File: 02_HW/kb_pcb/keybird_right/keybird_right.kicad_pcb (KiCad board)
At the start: 2 copper layers, 152.4 x 148.3 mm, 79 parts, among them J1 Adafruit_Feather_16_pin, J2 Adafruit_feather_12_pin, J4 FTDI UART, SW1 SW_Push, SW10 SW_Push, SW11 SW_Push, SW12 SW_Push, SW13 SW_Push, SW14 SW_Push, SW15 SW_Push, SW16 SW_Push, SW17 SW_Push, SW18 SW_Push, SW19 SW_Push, SW2 SW_Push, SW20 SW_Push, SW21 SW_Push, SW22 SW_Push, SW23 SW_Push, SW24 SW_Push, SW25 SW_Push, SW26 SW_Push, SW27 SW_Push, SW28 SW_Push, SW29 SW_Push, SW3 SW_Push, SW30 SW_Push, SW4 SW_Push, SW5 Power enable, SW6 SW_Push, SW7 SW_Push, SW8 SW_Push, SW9 SW_Push

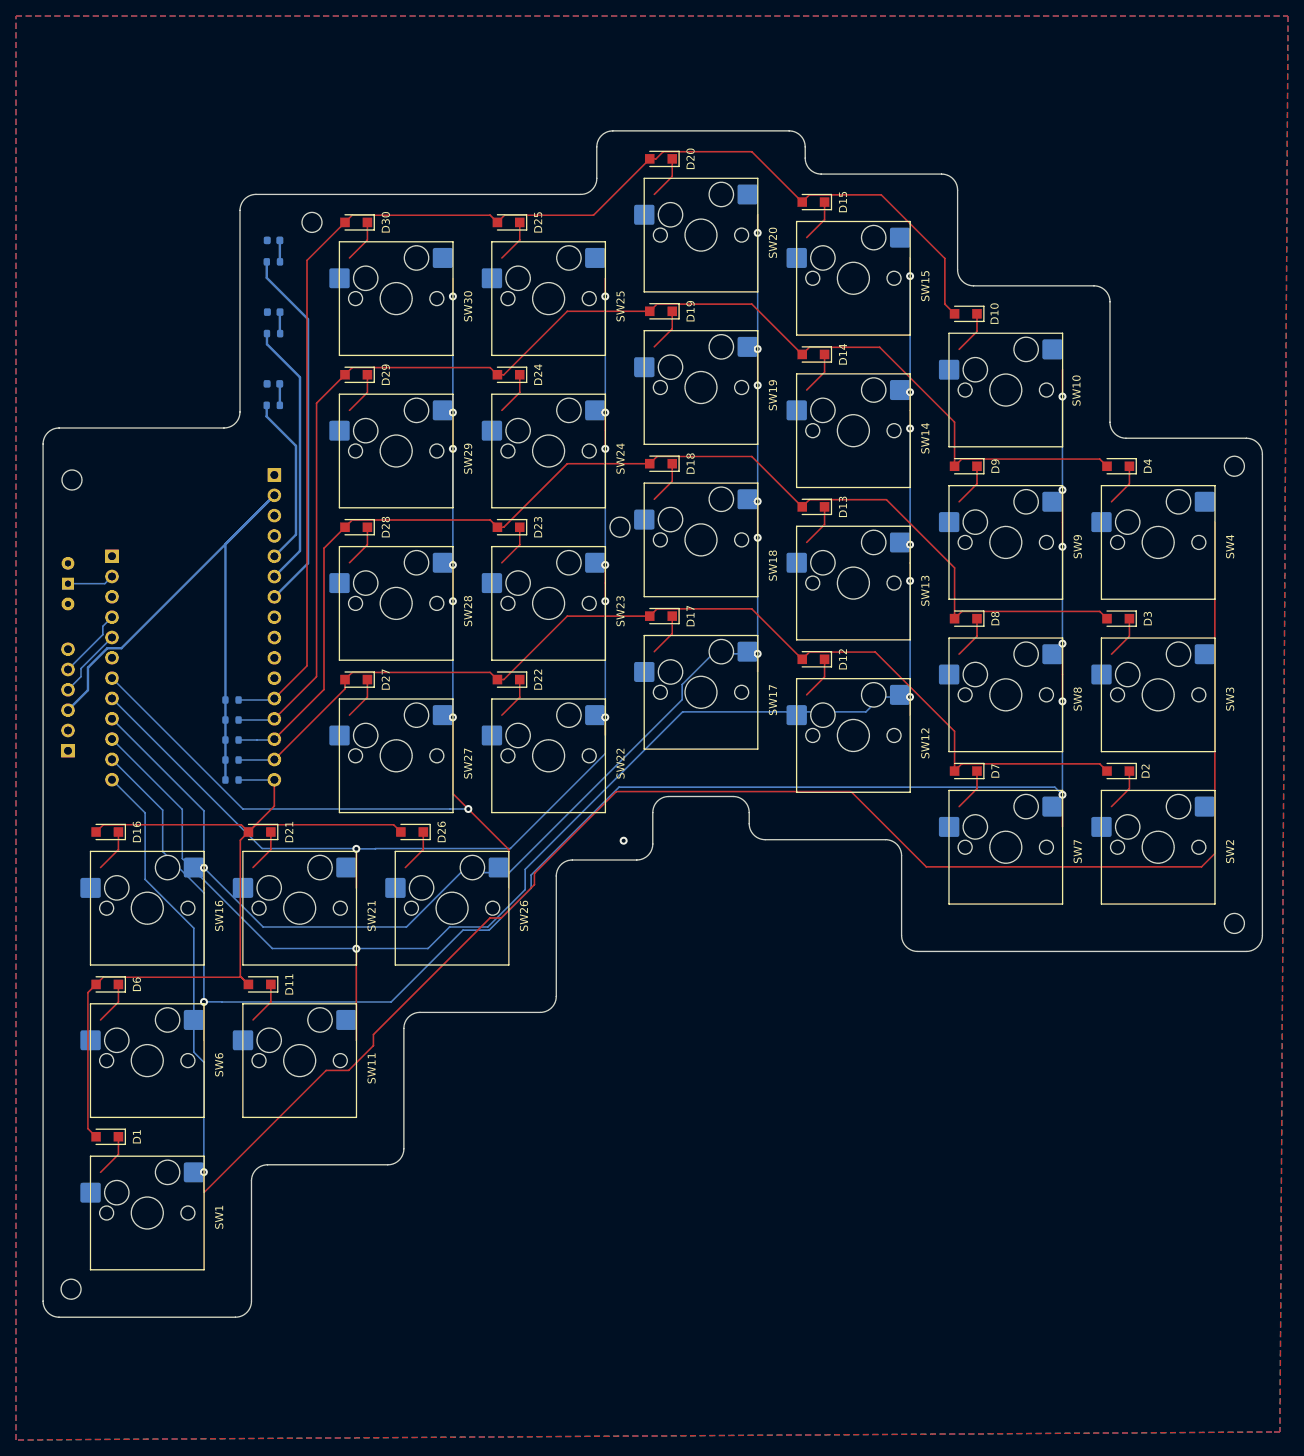
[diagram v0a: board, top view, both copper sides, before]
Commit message: left and right board pass design rule checks
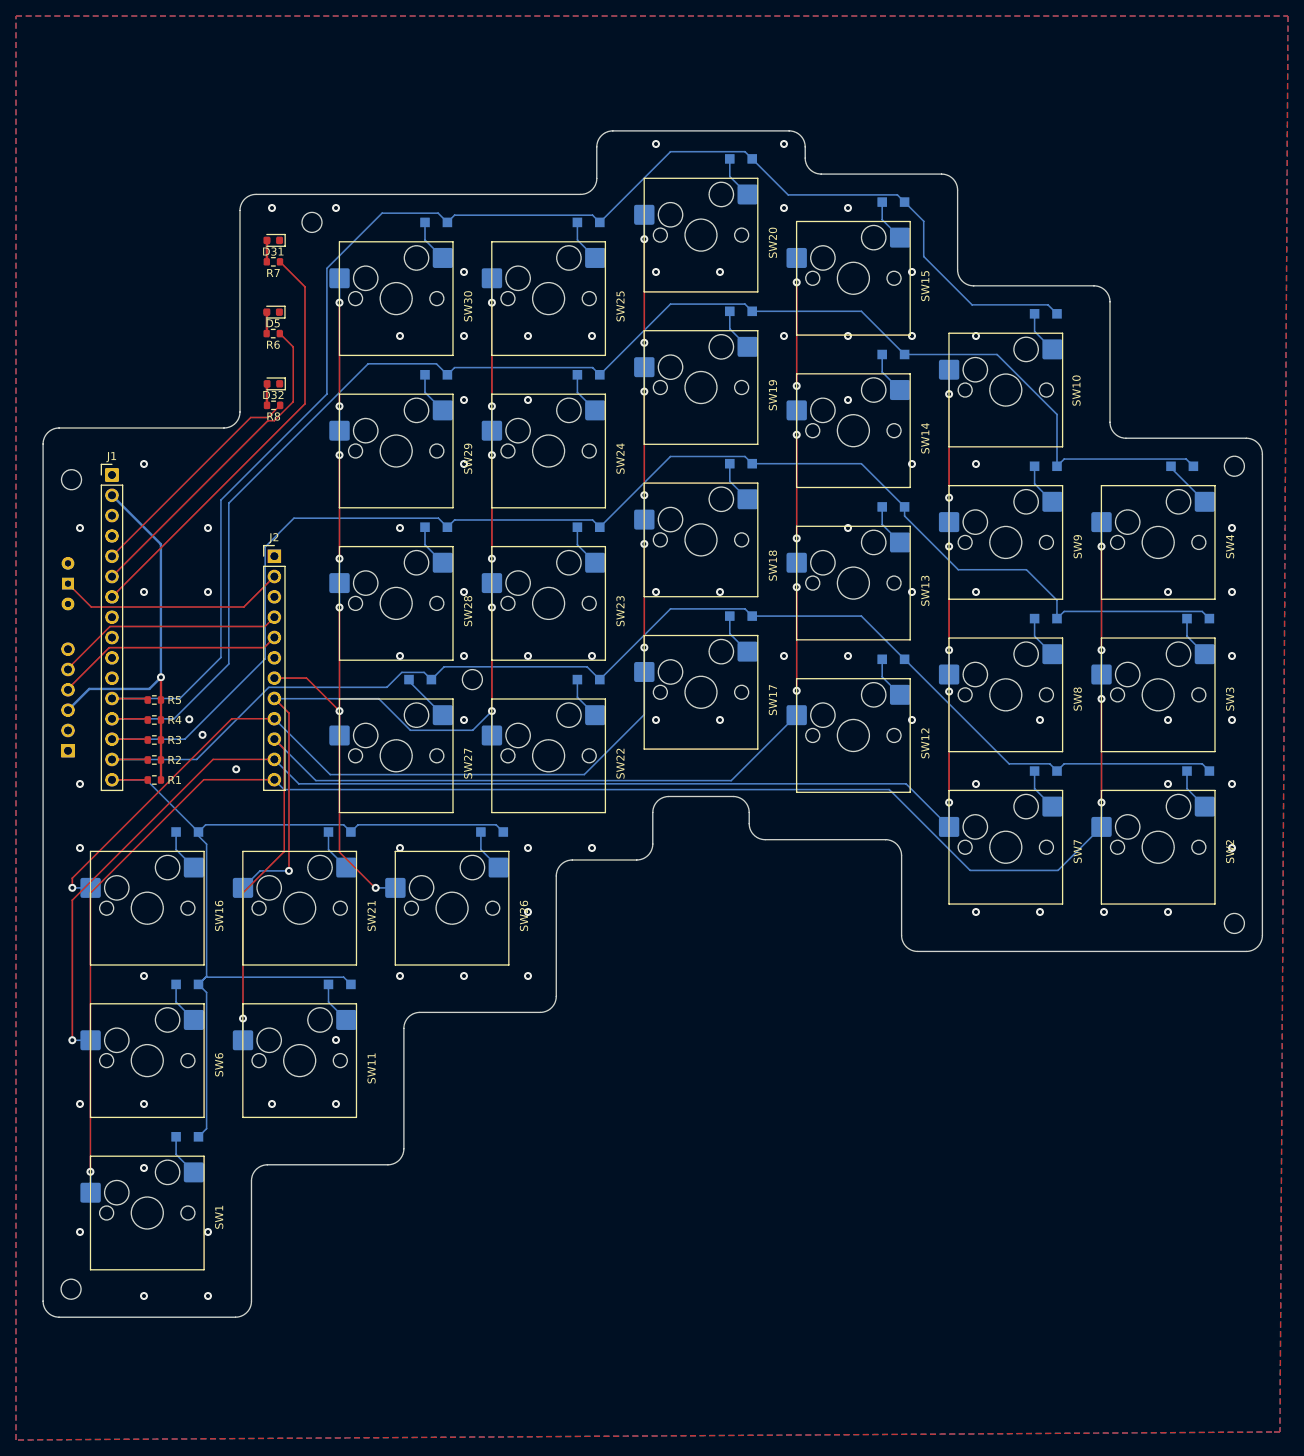
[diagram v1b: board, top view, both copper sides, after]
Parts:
- D1, D10, D11, D12, D13, D14, D15, D16, D17, D18, D19, D2, D20, D21, D22, D23, D24, D25, D26, D27, D28, D29, D3, D30, D4, D6, D7, D8, D9: moved to B.Cu
- D31, D32, D5, J1, J2, R1, R2, R3, R4, R5, R6, R7, R8: moved to F.Cu
- moved H4 26.5 mm to (154.1, 101.0)
- moved J1 20.3 mm to (109.0, 75.4), turned to 0 degrees
- moved J2 20.3 mm to (129.3, 85.5), turned to 0 degrees
- moved D10 10.0 mm to (225.7, 55.2), turned to 0 degrees
- moved D22 10.0 mm to (168.6, 101.0), turned to 0 degrees
- moved D23 10.0 mm to (168.6, 81.9), turned to 0 degrees
- moved D24 10.0 mm to (168.6, 62.9), turned to 0 degrees
- moved D26 10.0 mm to (156.5, 120.0), turned to 0 degrees
- moved D7 10.0 mm to (225.7, 112.4), turned to 0 degrees
- moved D8 10.0 mm to (225.7, 93.3), turned to 0 degrees
- moved D9 10.0 mm to (225.7, 74.3), turned to 0 degrees
- moved D1 10.0 mm to (118.4, 158.1), turned to 0 degrees
- moved D11 10.0 mm to (137.5, 139.1), turned to 0 degrees
- moved D16 10.0 mm to (118.4, 120.0), turned to 0 degrees
- moved D21 10.0 mm to (137.5, 120.0), turned to 0 degrees
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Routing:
- net /Col_5: track 130.6 -> 93.5 mm
- net /Col_0: track 251.2 -> 214.8 mm, vias 1 -> 5
- net /Row_1: track 130.6 -> 160.7 mm
- net /Row_2: track 147.9 -> 177.3 mm
- net /Col_2: track 197.3 -> 168.4 mm
- net +3.3V: track 76.8 -> 51.6 mm, vias 0 -> 1
- net /Col_4: track 141.2 -> 116.2 mm
- net /Row_3: track 164.0 -> 187.8 mm
- net /Row_4: track 160.8 -> 184.6 mm
- net /EN: track 5.87 -> 28.6 mm
- net /UART_TX: track 8.82 -> 28.6 mm
- net /UART_RX: track 8.82 -> 28.6 mm
- net /Col_1: track 216.9 -> 197.4 mm
- net /Col_3: track 170.9 -> 151.9 mm
- net /GREEN_LED: track 33.4 -> 40.9 mm
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
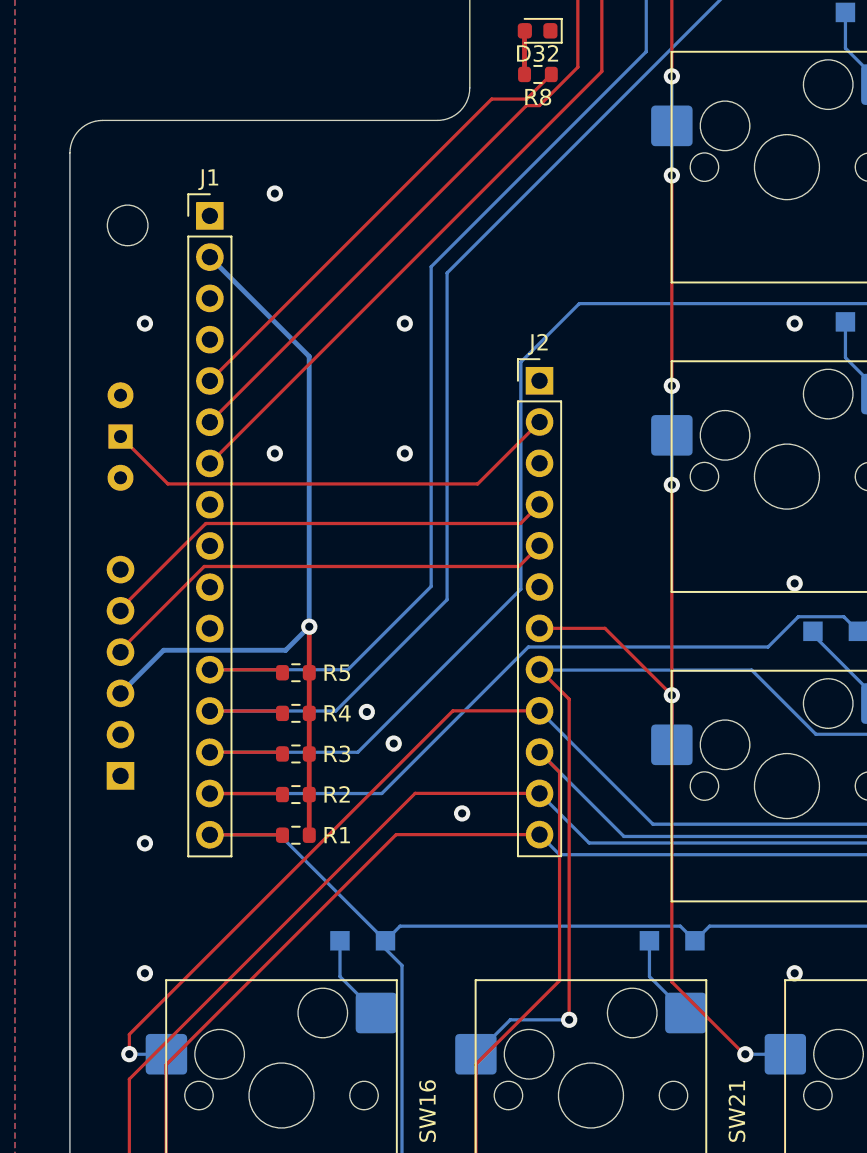
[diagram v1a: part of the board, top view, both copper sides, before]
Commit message: Left and right boards pass design rule checks
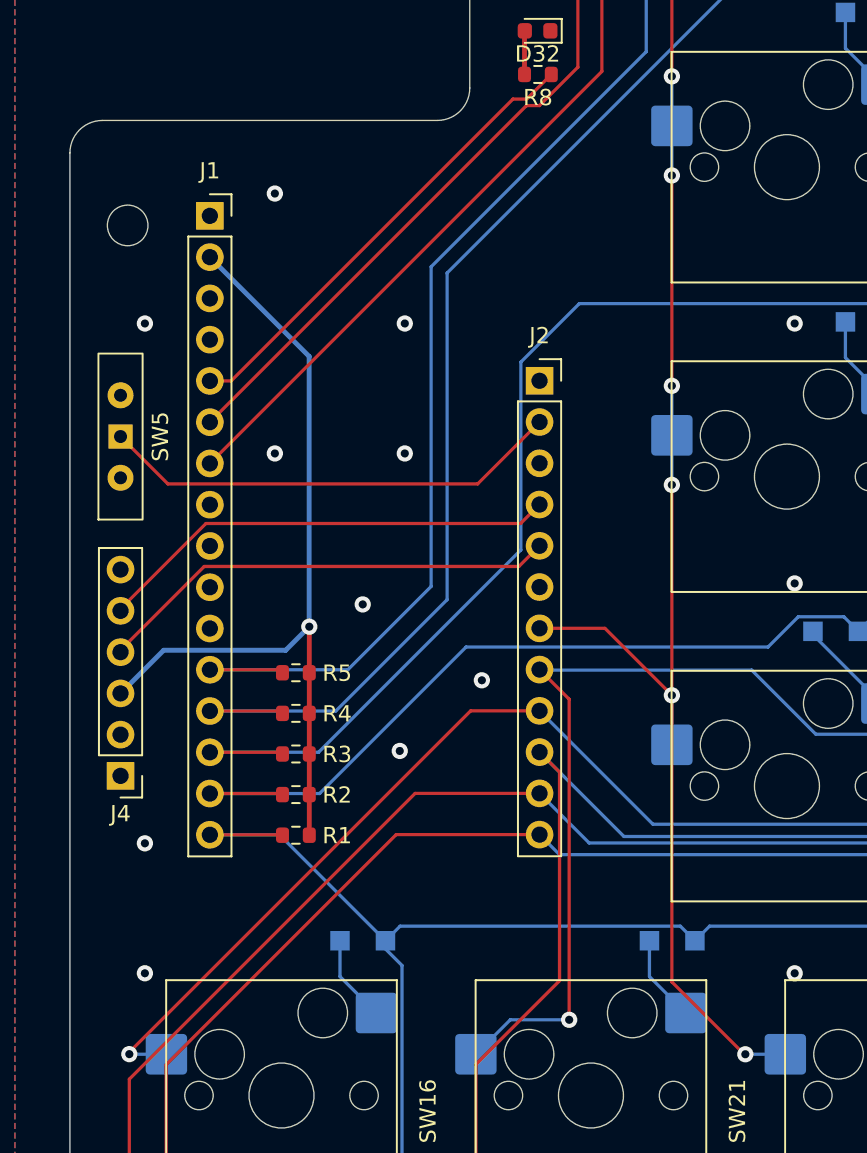
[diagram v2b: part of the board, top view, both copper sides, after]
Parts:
- J1: footprint Connector_PinHeader_2.54mm:PinHeader_1x16_P2.54mm_Vertical -> Connector_PinSocket_2.54mm:PinSocket_1x16_P2.54mm_Vertical
- J2: footprint Connector_PinHeader_2.54mm:PinHeader_1x12_P2.54mm_Vertical -> Connector_PinSocket_2.54mm:PinSocket_1x12_P2.54mm_Vertical
- J4, SW5: moved to F.Cu
- turned J4 to 180 degrees
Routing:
- net /Row_2: track 177.3 -> 175.9 mm
- net /Col_3: track 151.9 -> 151.3 mm
